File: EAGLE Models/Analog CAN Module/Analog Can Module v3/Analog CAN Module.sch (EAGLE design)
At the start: 257 parts, among them IC1 AT90CAN128, IC2 MCP2551SO8, IC3 NUP2105L, IC5 FT232RL, Q1 56P2859, U1 LTC2053, U10 LTC2053, U11 LTC2053, U12 LTC2053, U13 LTC2053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

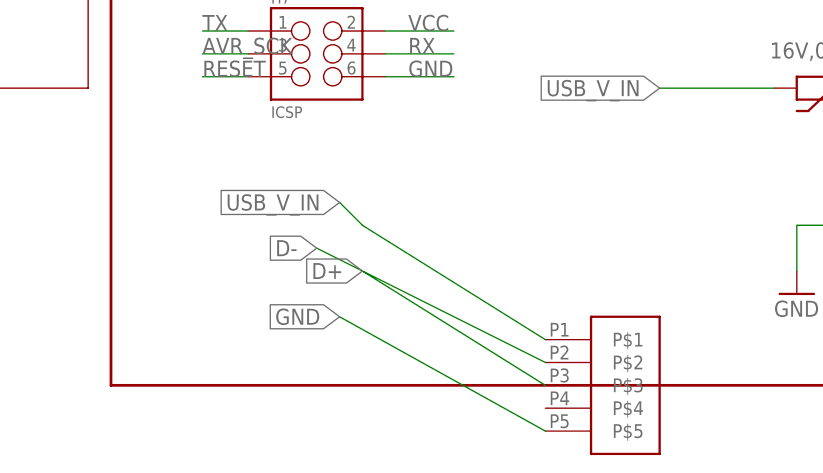
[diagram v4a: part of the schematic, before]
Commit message: Added the new usb connection and rerouted most of the traces
almost done, only a few more traces to go.
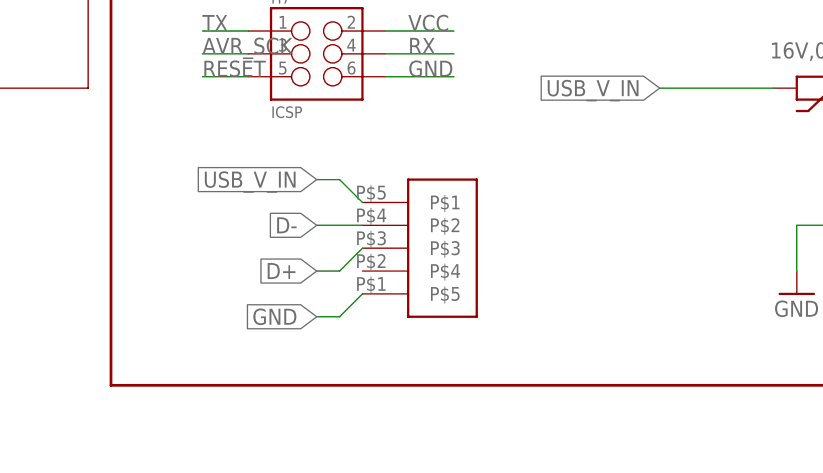
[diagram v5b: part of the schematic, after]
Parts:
- removed U$14: MUSBB, DashAndCAN library:MUSBB
- added U$3: 1734753-1, con-amp-te:1734753-1
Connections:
- net D+: now also U$3.P$3; no longer U$14.P$3
- net D-: now also U$3.P$2; no longer U$14.P$2
- net GND: now also U$3.P$5; no longer U$14.P$5
- net USB_V_IN: now also U$3.P$1; no longer U$14.P$1
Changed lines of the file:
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@@
 <part name="R78" library="SparkFun-Resistors" deviceset="RESISTOR" device="0603" value="10K"/>
 <part name="R79" library="SparkFun-Resistors" deviceset="RESISTOR" device="0603" value="1M"/>
-<part name="U$14" library="DashAndCAN library" deviceset="MUSBB" device=""/>
 <part name="X1" library="con-deutsch" deviceset="AS16-35" device=""/>
 <part name="U$13" library="DashAndCAN library" deviceset="AD7998" device=""/>
@@
 <part name="C14" library="rcl" deviceset="C-EU" device="C0805" value="22uF"/>
 <part name="C80" library="rcl" deviceset="C-EU" device="C0805" value="22uF"/>
+<part name="U$3" library="con-amp-te" deviceset="1734753-1" device=""/>
 </parts>
 <sheets>
@@
 <instance part="R78" gate="G$1" x="457.2" y="-30.48"/>
 <instance part="R79" gate="G$1" x="467.36" y="-38.1" rot="R90"/>
-<instance part="U$14" gate="G$1" x="68.58" y="-241.3"/>
 <instance part="X1" gate="/1" x="58.42" y="-124.46"/>
 <instance part="X1" gate="/2" x="58.42" y="-127"/>
@@
 <instance part="C14" gate="G$1" x="114.3" y="-162.56" rot="R90"/>
 <instance part="C80" gate="G$1" x="114.3" y="-172.72" rot="R90"/>
+<instance part="U$3" gate="G$1" x="48.26" y="-226.06"/>
 </instances>
 <busses>
@@
 </segment>
 <segment>
-<pinref part="U$14" gate="G$1" pin="P$5"/>
-<wire x1="60.96" y1="-246.38" x2="38.1" y2="-233.68" width="0.1524" layer="91"/>
-<label x="38.1" y="-233.68" size="1.778" layer="95" rot="R180" xref="yes"/>
+<label x="35.56" y="-233.68" size="1.778" layer="95" rot="R180" xref="yes"/>
+<pinref part="U$3" gate="G$1" pin="P$5"/>
+<wire x1="40.64" y1="-231.14" x2="38.1" y2="-233.68" width="0.1524" layer="91"/>
+<wire x1="38.1" y1="-233.68" x2="35.56" y2="-233.68" width="0.1524" layer="91"/>
 </segment>
 <segment>
@@
 </segment>
 <segment>
-<pinref part="U$14" gate="G$1" pin="P$2"/>
-<wire x1="60.96" y1="-238.76" x2="35.56" y2="-226.06" width="0.1524" layer="91"/>
-<label x="35.56" y="-226.06" size="1.778" layer="95" rot="R180" xref="yes"/>
+<label x="35.56" y="-223.52" size="1.778" layer="95" rot="R180" xref="yes"/>
+<pinref part="U$3" gate="G$1" pin="P$2"/>
+<wire x1="40.64" y1="-223.52" x2="35.56" y2="-223.52" width="0.1524" layer="91"/>
 </segment>
 </net>
@@
 </segment>
 <segment>
-<pinref part="U$14" gate="G$1" pin="P$3"/>
-<wire x1="60.96" y1="-241.3" x2="40.64" y2="-228.6" width="0.1524" layer="91"/>
-<label x="40.64" y="-228.6" size="1.778" layer="95" rot="R180" xref="yes"/>
+<label x="35.56" y="-228.6" size="1.778" layer="95" rot="R180" xref="yes"/>
+<pinref part="U$3" gate="G$1" pin="P$3"/>
+<wire x1="40.64" y1="-226.06" x2="38.1" y2="-228.6" width="0.1524" layer="91"/>
+<wire x1="38.1" y1="-228.6" x2="35.56" y2="-228.6" width="0.1524" layer="91"/>
 </segment>
 </net>
@@
 <net name="USB_V_IN" class="3">
 <segment>
-<pinref part="U$14" gate="G$1" pin="P$1"/>
-<wire x1="60.96" y1="-236.22" x2="40.64" y2="-223.52" width="0.1524" layer="91"/>
-<wire x1="40.64" y1="-223.52" x2="38.1" y2="-220.98" width="0.1524" layer="91"/>
-<label x="38.1" y="-220.98" size="1.778" layer="95" rot="R180" xref="yes"/>
-</segment>
-<segment>
+<label x="35.56" y="-218.44" size="1.778" layer="95" rot="R180" xref="yes"/>
+<pinref part="U$3" gate="G$1" pin="P$1"/>
+<wire x1="40.64" y1="-220.98" x2="38.1" y2="-218.44" width="0.1524" layer="91"/>
+<wire x1="38.1" y1="-218.44" x2="35.56" y2="-218.44" width="0.1524" layer="91"/>
+</segment>
+<segment>

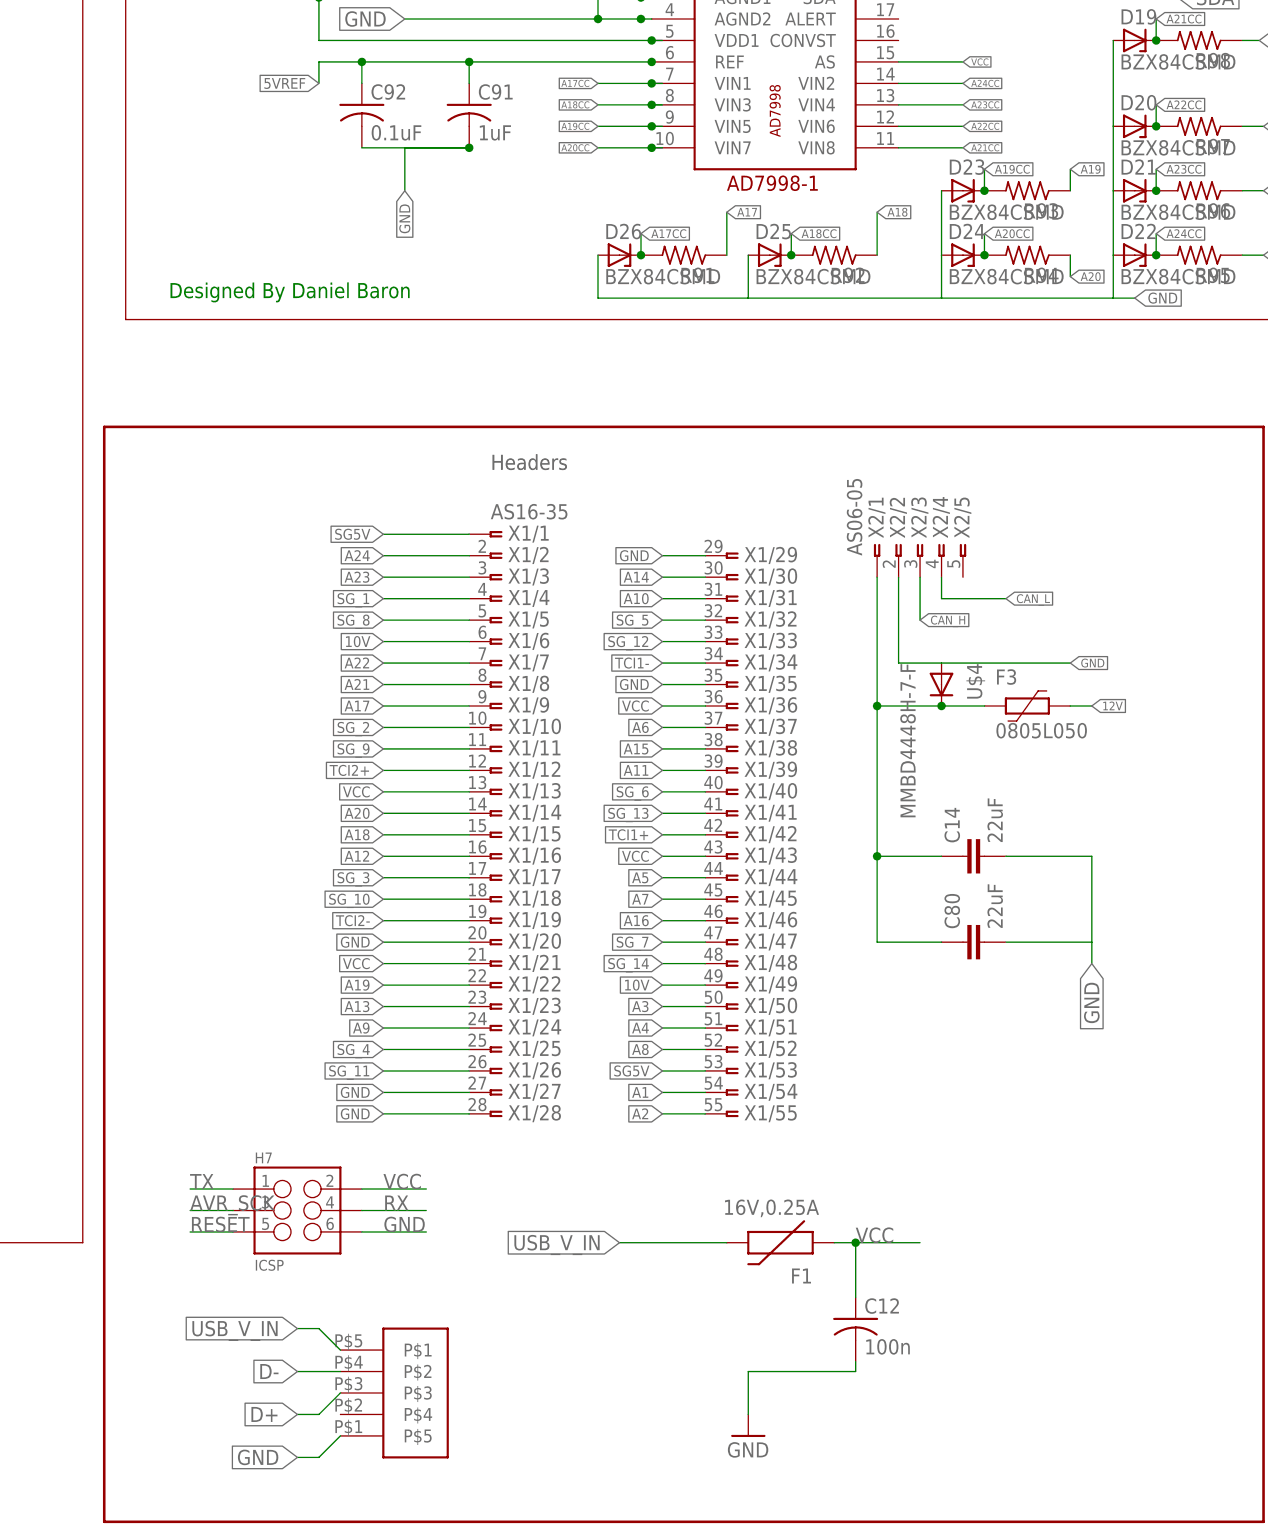
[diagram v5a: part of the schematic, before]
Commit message: Made the changes suggested by Daniel
Removed the USB, resized the SG traces, reworked gnd
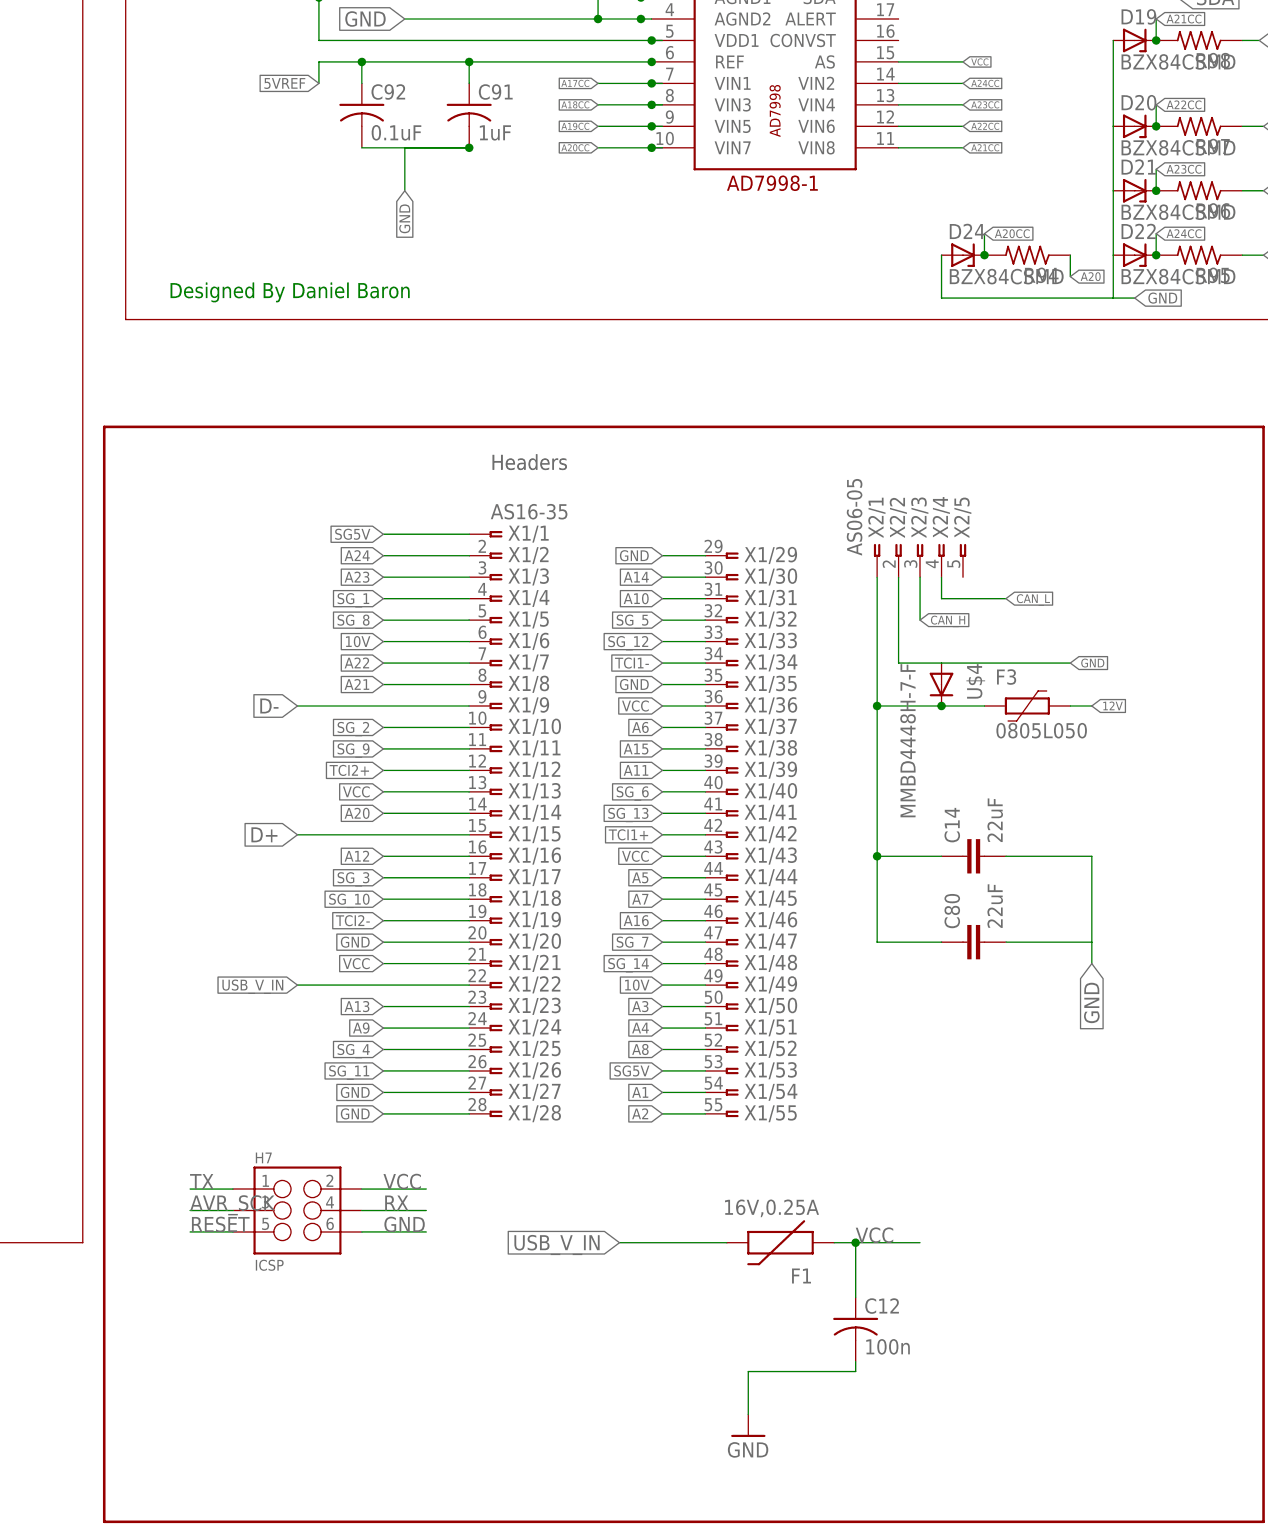
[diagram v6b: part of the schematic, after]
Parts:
- removed D23, D25, D26: BZX84CSMD, diode:BZX84CSMD
- removed R91, R92, R93: (no value), rcl:R-US_R0603
- removed U$3: 1734753-1, con-amp-te:1734753-1
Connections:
- removed net A17: R91.1, X1/9.1
- removed net A18: R92.1, X1/15.1
- removed net A19: R93.1, X1/22.1
- net A17CC: no longer D26.C, R91.2
- net A18CC: no longer D25.C, R92.2
- net A19CC: no longer D23.C, R93.2
- net D+: now also X1/15.1; no longer U$3.P$3
- net D-: now also X1/9.1; no longer U$3.P$2
- net GND: no longer D23.A, D25.A, D26.A, U$3.P$5
- net USB_V_IN: now also X1/22.1; no longer U$3.P$1
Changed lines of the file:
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@@
 <part name="D21" library="diode" deviceset="BZX84CSMD" device=""/>
 <part name="D22" library="diode" deviceset="BZX84CSMD" device=""/>
-<part name="D23" library="diode" deviceset="BZX84CSMD" device=""/>
 <part name="D24" library="diode" deviceset="BZX84CSMD" device=""/>
-<part name="D25" library="diode" deviceset="BZX84CSMD" device=""/>
-<part name="D26" library="diode" deviceset="BZX84CSMD" device=""/>
 <part name="U$4" library="diodes-inc" deviceset="MMBD4448H-7-F" device=""/>
 <part name="F3" library="LittleFuse" deviceset="?" device="0805L" technology="050"/>
@@
 <part name="R89" library="rcl" deviceset="R-US_" device="R0603"/>
 <part name="R90" library="rcl" deviceset="R-US_" device="R0603"/>
-<part name="R91" library="rcl" deviceset="R-US_" device="R0603"/>
-<part name="R92" library="rcl" deviceset="R-US_" device="R0603"/>
-<part name="R93" library="rcl" deviceset="R-US_" device="R0603"/>
 <part name="R94" library="rcl" deviceset="R-US_" device="R0603"/>
 <part name="R95" library="rcl" deviceset="R-US_" device="R0603"/>
@@
 <part name="C14" library="rcl" deviceset="C-EU" device="C0805" value="22uF"/>
 <part name="C80" library="rcl" deviceset="C-EU" device="C0805" value="22uF"/>
-<part name="U$3" library="con-amp-te" deviceset="1734753-1" device=""/>
 </parts>
 <sheets>
@@
 <instance part="D21" gate="G$1" x="134.62" y="-83.82"/>
 <instance part="D22" gate="G$1" x="134.62" y="-91.44"/>
-<instance part="D23" gate="G$1" x="114.3" y="-83.82"/>
 <instance part="D24" gate="G$1" x="114.3" y="-91.44"/>
-<instance part="D25" gate="G$1" x="91.44" y="-91.44"/>
-<instance part="D26" gate="G$1" x="73.66" y="-91.44"/>
 <instance part="U$4" gate="G$1" x="111.76" y="-142.24" rot="R270"/>
 <instance part="F3" gate="G$1" x="121.92" y="-144.78"/>
@@
 <instance part="R89" gate="G$1" x="83.82" y="-30.48" rot="R180"/>
 <instance part="R90" gate="G$1" x="83.82" y="-38.1" rot="R180"/>
-<instance part="R91" gate="G$1" x="81.28" y="-91.44" rot="R180"/>
-<instance part="R92" gate="G$1" x="99.06" y="-91.44" rot="R180"/>
-<instance part="R93" gate="G$1" x="121.92" y="-83.82" rot="R180"/>
 <instance part="R94" gate="G$1" x="121.92" y="-91.44" rot="R180"/>
 <instance part="R95" gate="G$1" x="142.24" y="-91.44" rot="R180"/>
@@
 <instance part="C14" gate="G$1" x="114.3" y="-162.56" rot="R90"/>
 <instance part="C80" gate="G$1" x="114.3" y="-172.72" rot="R90"/>
-<instance part="U$3" gate="G$1" x="48.26" y="-226.06"/>
 </instances>
 <busses>
@@
 </segment>
 <segment>
-<label x="35.56" y="-233.68" size="1.778" layer="95" rot="R180" xref="yes"/>
-<pinref part="U$3" gate="G$1" pin="P$5"/>
-<wire x1="40.64" y1="-231.14" x2="38.1" y2="-233.68" width="0.1524" layer="91"/>
-<wire x1="38.1" y1="-233.68" x2="35.56" y2="-233.68" width="0.1524" layer="91"/>
-</segment>
-<segment>
 <wire x1="77.47" y1="-60.96" x2="76.2" y2="-60.96" width="0.1524" layer="91"/>
 <wire x1="76.2" y1="-60.96" x2="71.12" y2="-60.96" width="0.1524" layer="91"/>
@@
 </segment>
 <segment>
-<pinref part="D26" gate="G$1" pin="A"/>
-<wire x1="71.12" y1="-91.44" x2="71.12" y2="-96.52" width="0.1524" layer="91"/>
-<wire x1="71.12" y1="-96.52" x2="88.9" y2="-96.52" width="0.1524" layer="91"/>
-<pinref part="D25" gate="G$1" pin="A"/>
-<wire x1="88.9" y1="-91.44" x2="88.9" y2="-96.52" width="0.1524" layer="91"/>
 <pinref part="D24" gate="G$1" pin="A"/>
-<wire x1="88.9" y1="-96.52" x2="111.76" y2="-96.52" width="0.1524" layer="91"/>
 <wire x1="111.76" y1="-96.52" x2="111.76" y2="-91.44" width="0.1524" layer="91"/>
-<pinref part="D23" gate="G$1" pin="A"/>
-<wire x1="111.76" y1="-83.82" x2="111.76" y2="-91.44" width="0.1524" layer="91"/>
 <pinref part="D22" gate="G$1" pin="A"/>
 <wire x1="111.76" y1="-96.52" x2="132.08" y2="-96.52" width="0.1524" layer="91"/>
@@
 </segment>
 <segment>
-<label x="35.56" y="-223.52" size="1.778" layer="95" rot="R180" xref="yes"/>
-<pinref part="U$3" gate="G$1" pin="P$2"/>
-<wire x1="40.64" y1="-223.52" x2="35.56" y2="-223.52" width="0.1524" layer="91"/>
+<pinref part="X1" gate="/9" pin="1"/>
+<wire x1="55.88" y1="-144.78" x2="35.56" y2="-144.78" width="0.1524" layer="91"/>
+<label x="35.56" y="-144.78" size="1.778" layer="95" rot="R180" xref="yes"/>
 </segment>
 </net>
@@
 </segment>
 <segment>
-<label x="35.56" y="-228.6" size="1.778" layer="95" rot="R180" xref="yes"/>
-<pinref part="U$3" gate="G$1" pin="P$3"/>
-<wire x1="40.64" y1="-226.06" x2="38.1" y2="-228.6" width="0.1524" layer="91"/>
-<wire x1="38.1" y1="-228.6" x2="35.56" y2="-228.6" width="0.1524" layer="91"/>
+<pinref part="X1" gate="/15" pin="1"/>
+<wire x1="55.88" y1="-160.02" x2="35.56" y2="-160.02" width="0.1524" layer="91"/>
+<label x="35.56" y="-160.02" size="1.778" layer="95" rot="R180" xref="yes"/>
 </segment>
 </net>
@@
 <net name="USB_V_IN" class="3">
 <segment>
-<label x="35.56" y="-218.44" size="1.778" layer="95" rot="R180" xref="yes"/>
-<pinref part="U$3" gate="G$1" pin="P$1"/>
-<wire x1="40.64" y1="-220.98" x2="38.1" y2="-218.44" width="0.1524" layer="91"/>
-<wire x1="38.1" y1="-218.44" x2="35.56" y2="-218.44" width="0.1524" layer="91"/>
-</segment>
-<segment>
 <pinref part="F1" gate="G$1" pin="2"/>
 <wire x1="86.36" y1="-208.28" x2="73.66" y2="-208.28" width="0.1524" layer="91"/>
 <label x="73.66" y="-208.28" size="1.778" layer="95" rot="R180" xref="yes"/>
 </segment>
+<segment>
+<pinref part="X1" gate="/22" pin="1"/>
+<wire x1="55.88" y1="-177.8" x2="35.56" y2="-177.8" width="0.1524" layer="91"/>
+<label x="35.56" y="-177.8" size="1.27" layer="95" rot="R180" xref="yes"/>
+</segment>
 </net>
 <net name="DTR" class="0">
@@
 </segment>
 </net>
-<net name="A17" class="0">
-<segment>
-<pinref part="X1" gate="/9" pin="1"/>
-<wire x1="55.88" y1="-144.78" x2="45.72" y2="-144.78" width="0.1524" layer="91"/>
-<label x="45.72" y="-144.78" size="1.27" layer="95" rot="R180" xref="yes"/>
-</segment>
-<segment>
-<pinref part="R91" gate="G$1" pin="1"/>
-<wire x1="86.36" y1="-91.44" x2="86.36" y2="-86.36" width="0.1524" layer="91"/>
-<label x="86.36" y="-86.36" size="1.016" layer="95" xref="yes"/>
-</segment>
-</net>
-<net name="A18" class="0">
-<segment>
-<pinref part="X1" gate="/15" pin="1"/>
-<wire x1="55.88" y1="-160.02" x2="45.72" y2="-160.02" width="0.1524" layer="91"/>
-<label x="45.72" y="-160.02" size="1.27" layer="95" rot="R180" xref="yes"/>
-</segment>
-<segment>
-<pinref part="R92" gate="G$1" pin="1"/>
-<wire x1="104.14" y1="-91.44" x2="104.14" y2="-86.36" width="0.1524" layer="91"/>
-<label x="104.14" y="-86.36" size="1.016" layer="95" xref="yes"/>
-</segment>
-</net>
-<net name="A19" class="0">
-<segment>
-<pinref part="X1" gate="/22" pin="1"/>
-<wire x1="55.88" y1="-177.8" x2="45.72" y2="-177.8" width="0.1524" layer="91"/>
-<label x="45.72" y="-177.8" size="1.27" layer="95" rot="R180" xref="yes"/>
-</segment>
-<segment>
-<pinref part="R93" gate="G$1" pin="1"/>
-<wire x1="127" y1="-83.82" x2="127" y2="-81.28" width="0.1524" layer="91"/>
-<label x="127" y="-81.28" size="1.016" layer="95" xref="yes"/>
-</segment>
-</net>
 <net name="A20" class="0">
 <segment>
@@
 <net name="A19CC" class="0">
 <segment>
-<pinref part="D23" gate="G$1" pin="C"/>
-<pinref part="R93" gate="G$1" pin="2"/>
-<wire x1="116.84" y1="-83.82" x2="116.84" y2="-81.28" width="0.1524" layer="91"/>
-<junction x="116.84" y="-83.82"/>
-<label x="116.84" y="-81.28" size="1.016" layer="95" xref="yes"/>
-</segment>
-<segment>
 <wire x1="78.74" y1="-76.2" x2="77.47" y2="-76.2" width="0.1524" layer="91"/>
 <label x="71.12" y="-76.2" size="0.8128" layer="95" rot="R180" xref="yes"/>
@@
 <net name="A17CC" class="0">
 <segment>
-<pinref part="D26" gate="G$1" pin="C"/>
-<pinref part="R91" gate="G$1" pin="2"/>
-<wire x1="76.2" y1="-91.44" x2="76.2" y2="-88.9" width="0.1524" layer="91"/>
-<junction x="76.2" y="-91.44"/>
-<label x="76.2" y="-88.9" size="1.016" layer="95" xref="yes"/>
-</segment>
-<segment>
 <wire x1="78.74" y1="-71.12" x2="77.47" y2="-71.12" width="0.1524" layer="91"/>
 <label x="71.12" y="-71.12" size="0.8128" layer="95" rot="R180" xref="yes"/>
@@
 <net name="A18CC" class="0">
 <segment>
-<pinref part="D25" gate="G$1" pin="C"/>
-<pinref part="R92" gate="G$1" pin="2"/>
-<wire x1="93.98" y1="-91.44" x2="93.98" y2="-88.9" width="0.1524" layer="91"/>
-<junction x="93.98" y="-91.44"/>
-<label x="93.98" y="-88.9" size="1.016" layer="95" xref="yes"/>
-</segment>
-<segment>
 <wire x1="78.74" y1="-73.66" x2="77.47" y2="-73.66" width="0.1524" layer="91"/>
